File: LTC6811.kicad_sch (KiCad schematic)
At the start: 60 parts, among them J16 Conn_01x01, J20 Conn_01x01, J21 Conn_01x01, J22 Conn_01x01, J23 BAT1, J26 Temp, J27 BAT2, Q10 NSV1C201MZ4, U11 LTC6811HG-1

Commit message: Add files via upload
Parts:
- removed LOGO2: Logo_Open_Hardware_Small, ENNOID:ENNOID-LOGO, symbol Graphic:Logo_Open_Hardware_Small
- removed U18: ~, symbol Fiber_Optic:logo
- J10: renamed from J20; footprint Mounting_Holes:MountingHole_3.2mm_M3_ISO7380_Pad -> MountingHole:MountingHole_3.2mm_M3_ISO7380_Pad
- J11: renamed from J21; footprint Mounting_Holes:MountingHole_3.2mm_M3_ISO7380_Pad -> MountingHole:MountingHole_3.2mm_M3_ISO7380_Pad
- J12: renamed from J22; footprint Mounting_Holes:MountingHole_3.2mm_M3_ISO7380_Pad -> MountingHole:MountingHole_3.2mm_M3_ISO7380_Pad
- J13: renamed from J27; footprint (none) -> Connector_JST:JST_XH_B7B-XH-A_1x07_P2.50mm_Vertical_BAT_6S
- J14: renamed from J23; footprint (none) -> Connector_JST:JST_XH_B7B-XH-A_1x07_P2.50mm_Vertical_BAT_6S
- J9: renamed from J16; footprint Mounting_Holes:MountingHole_3.2mm_M3_ISO7380_Pad -> MountingHole:MountingHole_3.2mm_M3_ISO7380_Pad
- renumbered C23 to C46, C24 to C47, C25 to C48, C26 to C49, C27 to C50, C28 to C51, C29 to C52, C30 to C53, C32 to C54, C33 to C55, C34 to C56, C35 to C57, C36 to C58, D19 to D10, D22 to D11, D23 to D12, D6 to D9, F9 to F10, F10 to F11, F11 to F12, F12 to F13, F13 to F14, F14 to F7, F7 to F8, F8 to F9, J26 to J15, Q10 to Q2, R12 to R53, R18 to R54, R48 to R55, R49 to R56, R51 to R57, R8 to R58, R52 to R59, R53 to R60, R55 to R61, R56 to R62, R57 to R63, R58 to R64, R59 to R65, R60 to R66, R61 to R67, TH2 to TH1, U11 to U12
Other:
- company: (none) -> teTra

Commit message: Add files via upload
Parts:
- removed D12: LED, LED_SMD:LED_0603_1608Metric, symbol LTC6811-rescue:LED-Device
- removed J15: Temp, Connector_PinHeader_2.54mm:PinHeader_1x05_P2.54mm_Vertical, symbol LTC6811-rescue:Conn_01x05_Male-Connector
- added D12: LED Red, LED_SMD:LED_0603_1608Metric, symbol Device:LED
- added TH2, TH3, TH4, TH5: 100K, Resistor_SMD:R_0805_2012Metric, symbol Device:Thermistor
- C46, C47, C50, C51, C52: value 1u -> 1uF 25V; footprint Capacitor_SMD:C_0805_2012Metric -> Capacitor_SMD:C_0603_1608Metric; Link (none) -> https://www.digikey.jp/en/products/detail/nextgen-component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; MPN CL21B105KBFNNNE -> 0603B105K250XD
- C48, C49, C54, C55, C56, C57, C58: value 100n -> 100nF 100V; Link (none) -> https://www.digikey.jp/en/products/detail/samsung-electro-m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; MPN CC0603KRX7R0BB104 -> CL10B104KC8NNNC
- C53: value 100p -> 100pF 100V; Link (none) -> https://www.digikey.jp/en/products/detail/nextgen-component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; MPN CL10C101JB8NNNC -> 0603B101K101SD
- D10, D9: Link (none) -> https://www.digikey.jp/en/products/detail/diodes-incorporat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
- D11: footprint Diode_SMD:D_SOD-123 -> Diode_SMD:D_SOD-123F; Link (none) -> https://www.digikey.jp/en/products/detail/nexperia-usa-inc/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
- F1, F10, F11, F12, F13, F14, F2, F3, F4, F5, F6, F7, F8, F9: value 0.25A -> MPZ2012S102ATD25; footprint ENNOID:FUSE -> Fuse:Fuse_0805_2012Metric; Link (none) -> https://www.digikey.jp/en/products/detail/tdk-corporation/M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; MPN N/A -> MPZ2012S102ATD25
- FB1: value 33 -> BLM18PG330SN1D; Link (none) -> https://www.digikey.jp/en/products/detail/murata-electronic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
- J10, J11, J12, J9: value Conn_01x01 -> Hole /NC
- J13: value BAT2 -> B7B-XH-A; Link (none) -> https://www.digikey.jp/en/products/detail/jst-sales-america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; MPN (none) -> B7B-XH-A
- J14: value BAT1 -> B7B-XH-A; Link (none) -> https://www.digikey.jp/en/products/detail/jst-sales-america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; MPN (none) -> B7B-XH-A
- R53, R54, R61: value 100 -> 100R
- R58, R62, R63, R64, R65, R67: value 100k -> 100K
- R59, R66: value 1.2k -> 1.2K
- R60: value 806 -> 806R
- TH1: value 100k -> 100K NTC; footprint Resistor_SMD:R_0805_2012Metric -> Resistor_SMD:R_0603_1608Metric; Link (none) -> https://www.digikey.jp/en/products/detail/epcos-tdk-electro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; MPN SDNT2012X104F4250FTF -> B57355V5104F360
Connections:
- net GND_PACK: now also TH2.2, TH3.2, TH4.2, TH5.2
- net T2: now also TH2.1
- net T3: now also TH3.1
- net T4: now also TH4.1
- net T5: now also TH5.1
- net Vreg: now also D12.2 (A)
- net at R66.1: now also D12.1 (K)
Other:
- moved on the sheet: R55, R56, R57

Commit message: Add files via upload
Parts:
- Q2: Link (none) -> https://www.digikey.jp/en/products/detail/onsemi/NSV1C201MZ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
- R53, R54, R60, R61: Link (none) -> https://www.digikey.jp/en/products/detail/yageo/RC0603FR-07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
- R55, R56, R57, R58, R59, R62, R63, R64, R65, R66, R67: Link (none) -> https://www.digikey.jp/en/products/detail/yageo/RC0603JR-07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
- TH2, TH3, TH4, TH5: value 100K -> 100K NTC; footprint Resistor_SMD:R_0805_2012Metric -> Resistor_THT:R_Axial_DIN0204_L3.6mm_D1.6mm_P1.90mm_Vertical; Link https://www.digikey.jp/en/products/detail/cantherm/MF52A110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 -> https://www.digikey.jp/en/products/detail/cantherm/MF52C110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; MPN MF52A1104J3950 -> MF52C1104F4150
- TR2: Link (none) -> https://www.digikey.jp/en/products/detail/pulse-electronics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
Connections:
- net C_1 renamed C1_G
- net C_2 renamed C2_G
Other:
- moved on the sheet: F1, F10, F11, F12, F13, F14, F2, F3, F4, F5, F6, F7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

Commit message: Add files via upload
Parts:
- removed J9: Hole /NC, MountingHole:MountingHole_3.2mm_M3_ISO7380_Pad, symbol Connector_Generic:Conn_01x01
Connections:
- no-connect marks 7 -> 6
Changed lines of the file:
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@@
   (junction (at 322.58 196.215) (diameter 0) (color 0 0 0 0)
   )
-  (no_connect (at 33.02 34.925))
   (no_connect (at 331.47 65.405))
   (no_connect (at 33.02 40.005))
@@
         )
       )
-    )
-  )
-  (symbol (lib_id "Connector_Generic:Conn_01x01") (at 27.94 34.925 180) (unit 1)
-    (in_bom yes) (on_board yes) (dnp no)
-    (property "Reference" "J9" (at 30.0228 31.5468 0)
-      (effects (font (size 1.27 1.27)))
-    )
-    (property "Value" "Hole /NC" (at 30.0228 31.5214 0)
-      (effects (font (size 1.27 1.27)) hide)
-    )
-    (property "Footprint" "MountingHole:MountingHole_3.2mm_M3_ISO7380_Pad" (at 27.94 34.925 0)
-      (effects (font (size 1.27 1.27)) hide)
-    )
-    (property "Datasheet" "~" (at 27.94 34.925 0)
-      (effects (font (size 1.27 1.27)) hide)
-    )
-    (property "MPN" "N/A" (at 27.94 34.925 0)
-      (effects (font (size 1.27 1.27)) hide)
-    )
-    (pin "1")
-    (instances
-      (project "LTC6811_ESP32"
-        (path "/6a86ff6f-b159-4c4c-8a40-e732cc82e010/0999518d-09c3-4a69-bd78-ff81b3ce8dd2"
-          (reference "J9") (unit 1)
-        )
-      )
-      (project "LTC6811"
-        (path "/c4061cfa-a05d-44c7-ba89-bb211c8b143a"
-          (reference "J7") (unit 1)
-        )
-      )

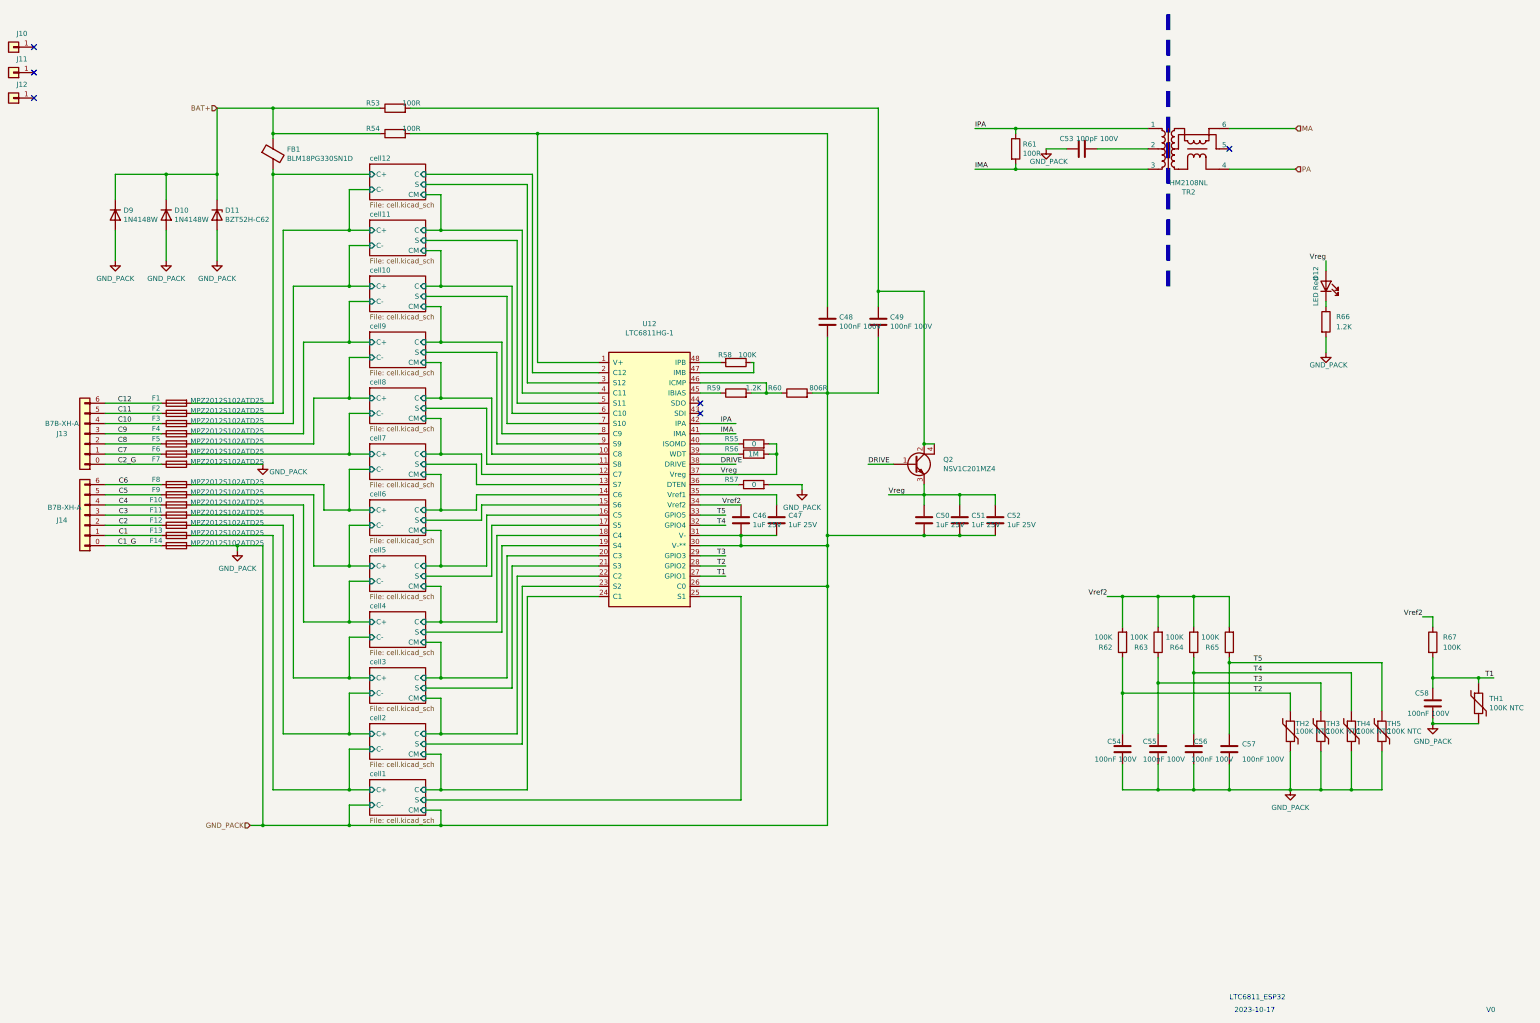
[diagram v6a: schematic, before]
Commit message: Add daisy chain connection interface.
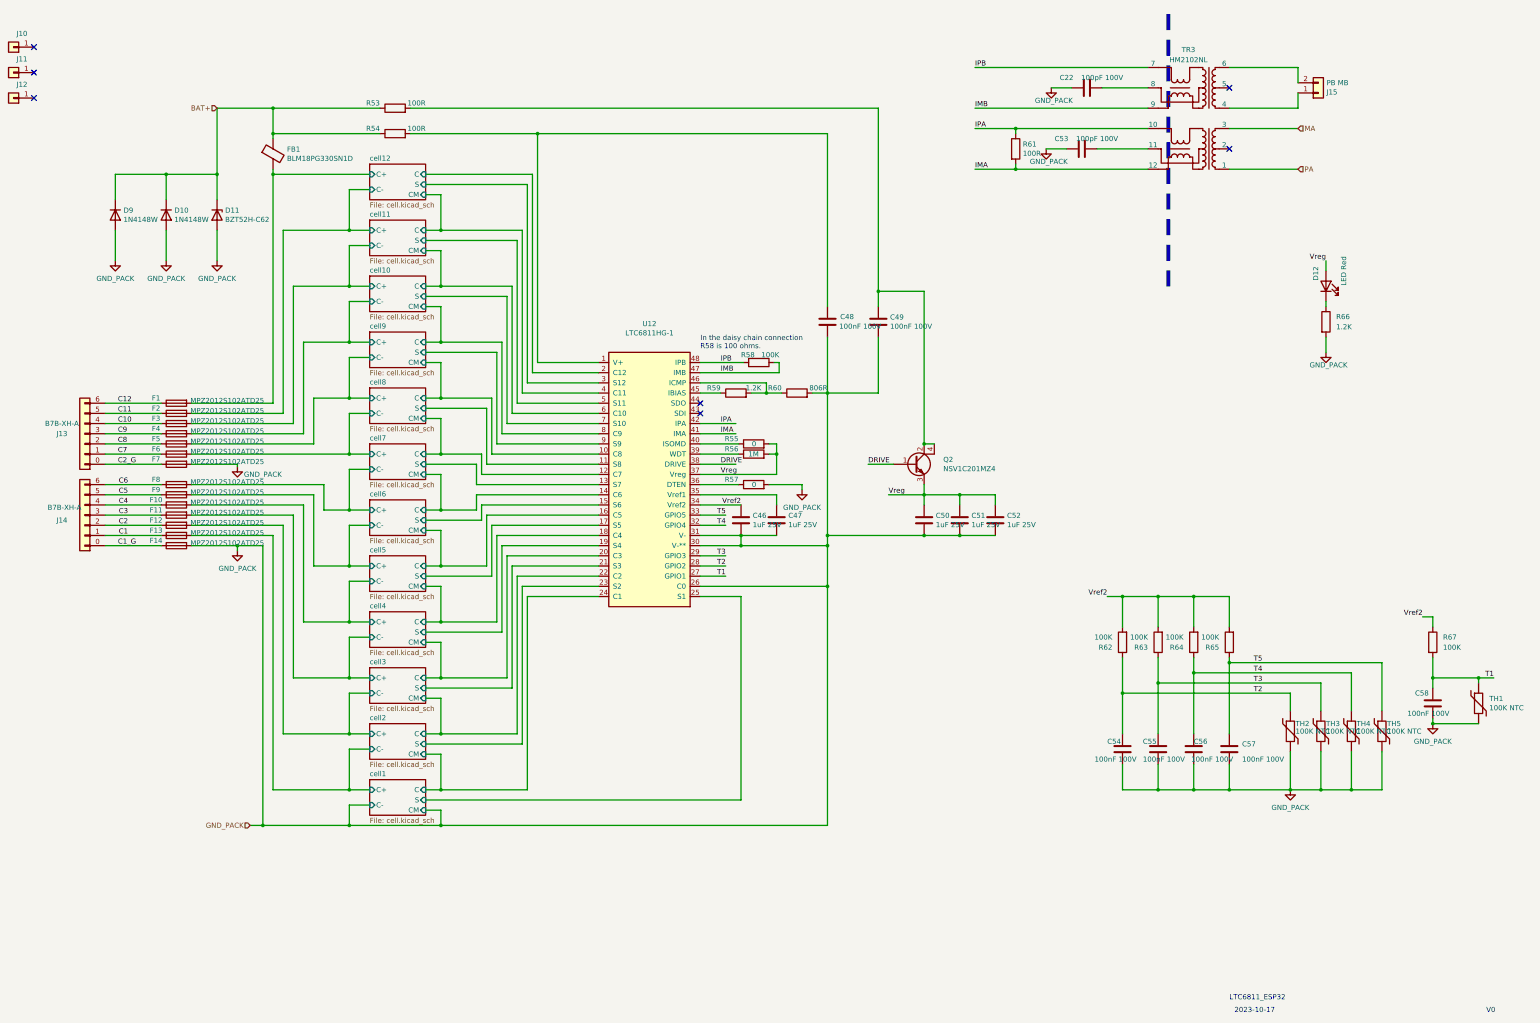
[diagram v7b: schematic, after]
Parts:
- removed TR2: HM2108NL, ENNOID:HM2108NL, symbol ENNOID:HM2108NL
- added C22: 100pF 100V, Capacitor_SMD:C_0603_1608Metric, symbol LTC6811-rescue:C-Device
- added J15: PB MB, ENNOID:Pin_1x02-XL, symbol Connector_Generic:Conn_01x02
- added TR3: HM2102NL, Transformer_SMD:HM2102NL_PUL, symbol Transformer:HM2102NL
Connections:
- net GND_PACK: now also C22.2
- net IMA: now also TR3.12
- net IPA: now also TR3.10
- net MA: now also TR3.3
- net PA: now also TR3.1
- net at C53.1: now also TR3.11
- net IMB: now reaches R58.1, U12.47 (IMB)
- net IMB: now also TR3.9
- net IPB: now reaches R58.2, U12.48 (IPB)
- net IPB: now also TR3.7
- new net: J15.1 (Pin_1), TR3.4
- new net: J15.2 (Pin_2), TR3.6
- new net: C22.1, TR3.8
- no-connect marks 6 -> 7
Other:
- note added: "In the daisy chain connection R58 is 100 ohms."
- moved on the sheet: R58
